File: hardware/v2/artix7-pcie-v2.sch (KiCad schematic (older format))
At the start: 51 parts, among them J10 USB_B_Micro, J3 JTAG_EN, J6 JTAG, J7 Conn_01x02, J8 SER, SW1 PROG, SW2 USER, U1 XC7A75T-FGG484, U2 W25Q64JVSSIM, U4 5P49V6965A000NLGI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

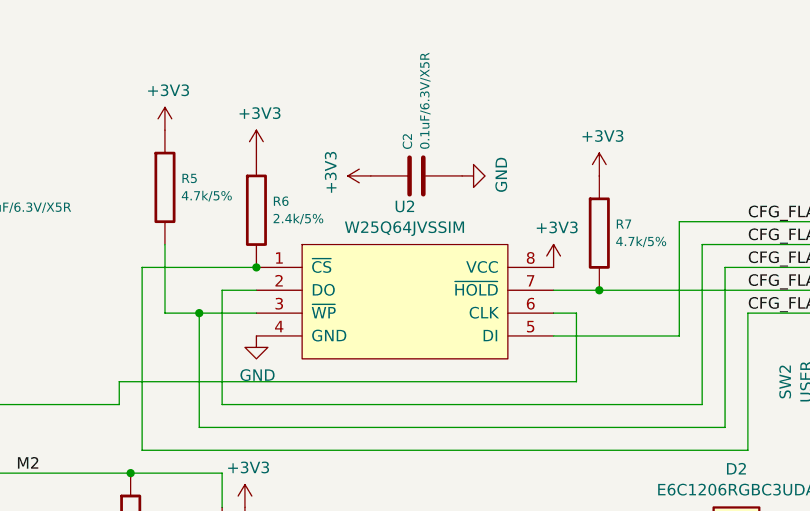
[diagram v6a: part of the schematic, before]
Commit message: v2 hardware: add Digikey part numbers to schematic and generate bom
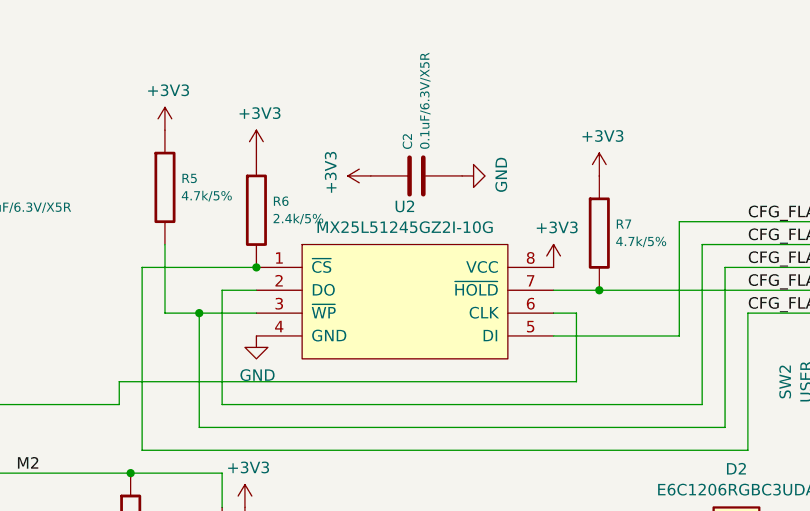
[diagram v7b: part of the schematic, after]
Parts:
- C1: Vendor (none) -> 587-3400-1-ND
- D2: Vendor (none) -> 754-2167-1-ND
- D3, D4: value SBR3U20SA-13‎ -> SBR3U20SA-13; Vendor (none) -> SBR3U20SA-13DICT-ND
- R2, R3, R5, R7: Vendor (none) -> 2019-RK73H1ETTP4701FCT-ND
- R29, R37: Vendor (none) -> 311-1.50KLRCT-ND
- R6: Vendor (none) -> YAG5283CT-ND
- U2: value W25Q64JVSSIM -> MX25L51245GZ2I-10G; Vendor (none) -> 1092-1247-ND
- U4: Vendor (none) -> 800-3818-ND
- X1: Vendor (none) -> 535-13468-6-ND
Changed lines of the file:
@@
 P 7050 1450
 F 0 "U2" H 7050 1865 50  0000 C CNN
-F 1 "W25Q64JVSSIM" H 7050 1774 50  0000 C CNN
+F 1 "MX25L51245GZ2I-10G" H 7050 1774 50  0000 C CNN
 F 2 "artix7-pcie-v2:WSON-8-1EP_8x6mm_P1.27mm" H 7350 1550 50  0001 C CNN
 F 3 "" H 7350 1550 50  0001 C CNN
+F 4 "1092-1247-ND" H 7050 1450 50  0001 C CNN "Vendor"
 	1    7050 1450
 	1    0    0    -1
@@
 F 2 "tom-passives:R_0402_1005Metric" V 7830 1150 30  0001 C CNN
 F 3 "" H 7900 1150 30  0000 C CNN
+F 4 "2019-RK73H1ETTP4701FCT-ND" H 7900 1150 50  0001 C CNN "Vendor"
 	1    7900 1150
 	1    0    0    -1
@@
 F 2 "tom-passives:R_0402_1005Metric" V 6330 1050 30  0001 C CNN
 F 3 "" H 6400 1050 30  0000 C CNN
+F 4 "YAG5283CT-ND" H 6400 1050 50  0001 C CNN "Vendor"
 	1    6400 1050
 	1    0    0    -1
@@
 F 2 "tom-passives:R_0402_1005Metric" V 5930 950 30  0001 C CNN
 F 3 "" H 6000 950 30  0000 C CNN
+F 4 "2019-RK73H1ETTP4701FCT-ND" H 6000 950 50  0001 C CNN "Vendor"
 	1    6000 950
 	1    0    0    -1
@@
 F 2 "tom-passives:C_1206_3216Metric" H 3338 650 30  0001 C CNN
 F 3 "" H 3300 800 60  0000 C CNN
+F 4 "587-3400-1-ND" H 3300 800 50  0001 C CNN "Vendor"
 	1    3300 800
 	1    0    0    -1
@@
 F 2 "tom-passives:R_0402_1005Metric" V 4930 3050 30  0001 C CNN
 F 3 "" H 5000 3050 30  0000 C CNN
+F 4 "2019-RK73H1ETTP4701FCT-ND" H 5000 3050 50  0001 C CNN "Vendor"
 	1    5000 3050
 	1    0    0    -1
@@
 F 2 "tom-passives:R_0402_1005Metric" V 4530 2950 30  0001 C CNN
 F 3 "" H 4600 2950 30  0000 C CNN
+F 4 "2019-RK73H1ETTP4701FCT-ND" H 4600 2950 50  0001 C CNN "Vendor"
 	1    4600 2950
 	1    0    0    -1
@@
 P 7750 5200
 F 0 "D3" H 7750 5084 40  0000 C CNN
-F 1 "SBR3U20SA-13‎" H 7750 5084 40  0001 C CNN
+F 1 "SBR3U20SA-13" H 7750 5084 40  0001 C CNN
 F 2 "tom-semiconductors:D_SMA" H 7750 5200 60  0001 C CNN
 F 3 "" H 7750 5200 60  0001 C CNN
+F 4 "SBR3U20SA-13DICT-ND" H 7750 5200 50  0001 C CNN "Vendor"
 	1    7750 5200
 	1    0    0    1
@@
 F 2 "tom-passives:R_0402_1005Metric" V 5780 6700 30  0001 C CNN
 F 3 "" H 5850 6700 30  0001 C CNN
+F 4 "311-1.50KLRCT-ND" H 5850 6700 50  0001 C CNN "Vendor"
 	1    5850 6700
 	-1   0    0    1
@@
 F 2 "tom-opto:E6C1206RGBC3UDA" H 8500 3200 50  0001 C CNN
 F 3 "https://datasheet.lcsc.com/szlcsc/1912111437_EKINGLUX-E6C1206RGBC3UDA_C375571.pdf" H 8500 2250 50  0001 C CNN
+F 4 "754-2167-1-ND" H 8500 2700 50  0001 C CNN "Vendor"
 	1    8500 2700
 	-1   0    0    -1
@@
 F 2 "tom-passives:R_0402_1005Metric" V 8880 3250 30  0001 C CNN
 F 3 "" H 8950 3250 30  0001 C CNN
+F 4 "311-1.50KLRCT-ND" H 8950 3250 50  0001 C CNN "Vendor"
 	1    8950 3250
 	0    1    1    0
@@
 P 8250 3350
 F 0 "D4" H 8250 3234 40  0000 C CNN
-F 1 "SBR3U20SA-13‎" H 8250 3234 40  0001 C CNN
+F 1 "SBR3U20SA-13" H 8250 3234 40  0001 C CNN
 F 2 "tom-semiconductors:D_SMA" H 8250 3350 60  0001 C CNN
 F 3 "" H 8250 3350 60  0001 C CNN
+F 4 "SBR3U20SA-13DICT-ND" H 8250 3350 50  0001 C CNN "Vendor"
 	1    8250 3350
 	1    0    0    1
@@
 F 8 "IDT" H 2550 6800 50  0001 L CNN "Manufacturer_Name"
 F 9 "5P49V6965A000NLGI" H 2550 6700 50  0001 L CNN "Manufacturer_Part_Number"
+F 10 "800-3818-ND" H 1300 6200 50  0001 C CNN "Vendor"
 	1    1300 6200
 	1    0    0    -1
@@
 F 2 "tom-passives:Crystal_SMD_3225-4Pin_3.2x2.5mm" V 644 6667 60  0001 R CNN
 F 3 "" H 750 6800 60  0001 C CNN
+F 4 "535-13468-6-ND" V 750 6800 50  0001 C CNN "Vendor"
 	1    750  6800
 	0    -1   -1   0

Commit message: hardware v2: bom fixes
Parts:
- X1: Vendor 535-13468-6-ND -> 535-13468-1-ND
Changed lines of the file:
@@
 F 2 "tom-passives:Crystal_SMD_3225-4Pin_3.2x2.5mm" V 644 6667 60  0001 R CNN
 F 3 "" H 750 6800 60  0001 C CNN
-F 4 "535-13468-6-ND" V 750 6800 50  0001 C CNN "Vendor"
+F 4 "535-13468-1-ND" V 750 6800 50  0001 C CNN "Vendor"
 	1    750  6800
 	0    -1   -1   0
